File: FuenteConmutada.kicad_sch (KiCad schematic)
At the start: 9 parts, among them J2 Conn_01x02_Socket, P1 USB_C_Plug_USB2.0, U1 MT3608

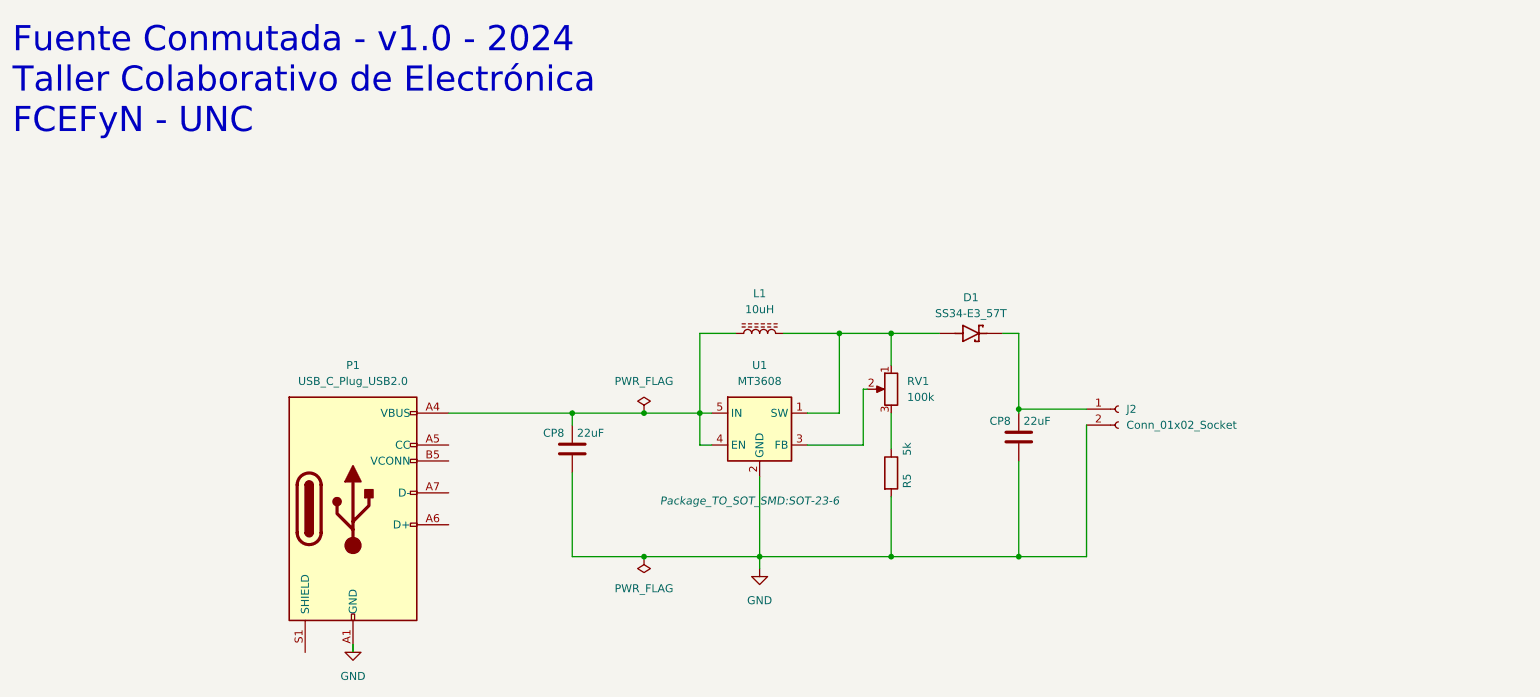
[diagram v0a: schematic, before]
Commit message: Esquematico 3in1 + Simbolo LMR64010 + Simu LT1930
Esquematico placa de prueba Boost-SEPIC-Fuente partida;
Simbolo para simulacion de LMR64010(xxx.asy debe estar en la misma carpeta);
Simulacion pasos del potenciometro, permite seleccionar el valor del pote(depende del valor de R2, L, RL)
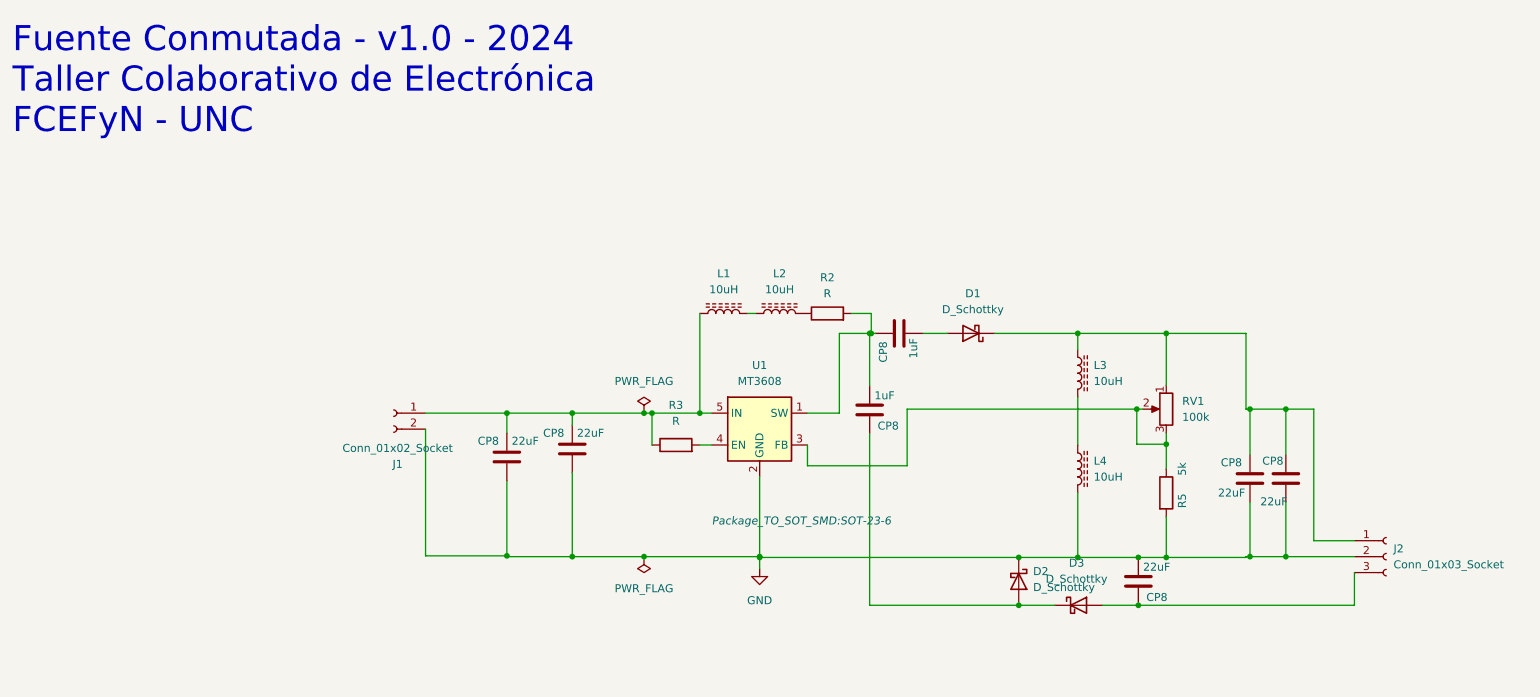
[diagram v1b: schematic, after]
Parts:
- removed D1: SS34-E3_57T, Diode_SMD:D_SMC_Handsoldering, symbol SS34-E3_57T:SS34-E3_57T
- removed J2: Conn_01x02_Socket, Connector_PinSocket_2.54mm:PinSocket_1x02_P2.54mm_Vertical, symbol Connector:Conn_01x02_Socket
- removed P1: USB_C_Plug_USB2.0, Connector_USB:USB_C_Receptacle_GCT_USB4105-xx-A_16P_TopMnt_Horizontal, symbol Connector:USB_C_Plug_USB2.0
- added CP8 (x2): 1uF, Capacitor_SMD:C_1206_3216Metric_Pad1.33x1.80mm_HandSolder, symbol Device:C
- added CP8 (x3): 22uF, Capacitor_SMD:C_1206_3216Metric_Pad1.33x1.80mm_HandSolder, symbol Device:C
- added D1, D2, D3: D_Schottky, Diode_SMD:D_SMA_Handsoldering, symbol Device:D_Schottky
- added J1: Conn_01x02_Socket, Connector_PinSocket_2.54mm:PinSocket_1x02_P2.54mm_Vertical, symbol Connector:Conn_01x02_Socket
- added J2: Conn_01x03_Socket, Connector_PinSocket_2.54mm:PinSocket_1x03_P2.54mm_Vertical, symbol Connector:Conn_01x03_Socket
- added L2, L3, L4: 10uH, Inductor_SMD:L_Taiyo-Yuden_NR-80xx_HandSoldering, symbol Device:L_Ferrite
- added R2, R3: R, Resistor_SMD:R_1206_3216Metric_Pad1.30x1.75mm_HandSolder, symbol Device:R
- RV1: footprint Potentiometer_THT:Potentiometer_Bourns_3299W_Vertical -> Potentiometer_THT:Potentiometer_Bourns_3299Y_Vertical
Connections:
- net GND: now also CP8.1, CP8.1, CP8.1, D2.1 (K), J1.2 (Pin_2), J2.2 (Pin_2), L4.2
- net at CP8.2: now also RV1.1, CP8.2, D1.1 (K), J2.1 (Pin_1), L3.1
- net at RV1.2, U1.3 (FB): now also R5.1, RV1.3
- net at CP8.2, L1.1, U1.5 (IN): now also CP8.2, J1.1 (Pin_1), R3.1; no longer U1.4 (EN)
- new net: L3.2, L4.1
- new net: CP8.1, CP8.2, R2.2, U1.1 (SW)
- new net: R3.2, U1.4 (EN)
- new net: CP8.2, D2.2 (A), D3.1 (K)
- new net: CP8.2, D3.2 (A), J2.3 (Pin_3)
- new net: CP8.1, D1.2 (A)
- new net: L1.2, L2.1
- new net: L2.2, R2.1
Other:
- moved on the sheet: CP8, L1, R5, RV1

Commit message: PCB
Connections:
- net Vo+: now reaches CP8.2, CP8.2, D1.1 (K), J2.1 (Pin_1), L3.1, RV1.1
- net Vin: now reaches CP8.2, CP8.2, J1.1 (Pin_1), L1.1, R3.1, U1.5 (IN)
- net Vo-: now reaches CP8.2, D3.2 (A), J2.3 (Pin_3)
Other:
- note added: "Inductor o Diodo (sepic o fuente partida)"
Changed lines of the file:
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@@
   (junction (at 200.025 63.5) (diameter 0) (color 0 0 0 0)
   )
+  (junction (at 219.075 99.06) (diameter 0) (color 0 0 0 0)
+  )
   (junction (at 105.41 76.2) (diameter 0) (color 0 0 0 0)
   )
@@
   (junction (at 176.53 99.187) (diameter 0) (color 0 0 0 0)
   )
-  (junction (at 219.075 99.06) (diameter 0) (color 0 0 0 0)
-  )
   (junction (at 125.73 76.2) (diameter 0) (color 0 0 0 0)
   )
@@
     (stroke (width 0) (type default))
   )
+  (wire (pts (xy 224.917 106.807) (xy 224.917 101.6))
+    (stroke (width 0) (type default))
+  )
   (wire (pts (xy 152.781 106.807) (xy 176.53 106.807))
     (stroke (width 0) (type default))
@@
     (stroke (width 0) (type default))
   )
+  (wire (pts (xy 125.73 60.325) (xy 125.73 76.2))
+    (stroke (width 0) (type default))
+  )
   (wire (pts (xy 105.41 76.2) (xy 116.84 76.2))
     (stroke (width 0) (type default))
   )
+  (wire (pts (xy 195.326 81.153) (xy 200.025 81.153))
+    (stroke (width 0) (type default))
+  )
+  (wire (pts (xy 94.996 86.995) (xy 94.996 98.933))
+    (stroke (width 0) (type default))
+  )
+  (wire (pts (xy 147.955 76.2) (xy 142.875 76.2))
+    (stroke (width 0) (type default))
+  )
+  (wire (pts (xy 185.928 63.5) (xy 200.025 63.5))
+    (stroke (width 0) (type default))
+  )
   (wire (pts (xy 219.075 99.06) (xy 229.997 99.06))
     (stroke (width 0) (type default))
   )
-  (wire (pts (xy 195.326 81.153) (xy 200.025 81.153))
-    (stroke (width 0) (type default))
-  )
-  (wire (pts (xy 94.996 86.995) (xy 94.996 98.933))
-    (stroke (width 0) (type default))
-  )
-  (wire (pts (xy 147.955 76.2) (xy 142.875 76.2))
-    (stroke (width 0) (type default))
-  )
-  (wire (pts (xy 185.928 63.5) (xy 200.025 63.5))
-    (stroke (width 0) (type default))
-  )
   (wire (pts (xy 185.928 73.66) (xy 185.928 81.28))
     (stroke (width 0) (type default))
@@
     (stroke (width 0) (type default))
   )
-  (wire (pts (xy 229.997 101.6) (xy 229.997 106.807))
+  (wire (pts (xy 224.917 106.807) (xy 195.58 106.807))
     (stroke (width 0) (type default))
   )
@@
     (stroke (width 0) (type default))
   )
-  (wire (pts (xy 229.997 106.807) (xy 195.58 106.807))
-    (stroke (width 0) (type default))
-  )
   (wire (pts (xy 94.996 76.2) (xy 94.996 79.375))
     (stroke (width 0) (type default))
@@
     (stroke (width 0) (type default))
   )
-  (wire (pts (xy 125.73 76.2) (xy 125.73 60.325))
-    (stroke (width 0) (type default))
-  )
   (wire (pts (xy 135.255 99.187) (xy 135.255 100.965))
     (stroke (width 0) (type default))
@@
   )
   (wire (pts (xy 118.11 76.2) (xy 118.11 81.28))
+    (stroke (width 0) (type default))
+  )
+  (wire (pts (xy 224.917 101.6) (xy 229.997 101.6))
     (stroke (width 0) (type default))
   )
@@
     (effects (font (size 4 4)) (justify left bottom))
   )
+  (text "Inductor o Diodo\n(sepic o fuente partida)" (at 168.656 90.932 0)
+    (effects (font (size 1.27 1.27)) (justify left bottom))
+  )
+  (label "Vo+" (at 227.203 96.52 0) (fields_autoplaced)
+    (effects (font (size 1.27 1.27)) (justify left bottom))
+  )
+  (label "Vin" (at 86.868 76.2 0) (fields_autoplaced)
+    (effects (font (size 1.27 1.27)) (justify left bottom))
+  )
+  (label "Vo-" (at 218.948 106.807 0) (fields_autoplaced)
+    (effects (font (size 1.27 1.27)) (justify left bottom))
+  )
   (symbol (lib_id "Device:L_Ferrite") (at 185.928 69.85 0) (unit 1)

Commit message: Cambios PCB+Esquematico
Huellas nuevas para inductores, diodos.
Correccion de diodo mal ubicado.
Se añadio R en serie con inductores 3 y 4, capacitor para compensacion, un segundo capacitor para salida Vo-.
Planos de GND, Vin, Vo+ y Vo-. Y tambien se agrandaron algunas pistas.
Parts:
- added CP8 (x2): 22uF, Capacitor_SMD:C_1206_3216Metric_Pad1.33x1.80mm_HandSolder, symbol Device:C
- added R4: R, Resistor_SMD:R_1206_3216Metric_Pad1.30x1.75mm_HandSolder, symbol Device:R
- D1, D2, D3: footprint Diode_SMD:D_SMA_Handsoldering -> Diode_SMD:D_SOD-128
- L1, L2, L3, L4: footprint Inductor_SMD:L_Taiyo-Yuden_NR-80xx_HandSoldering -> Inductor_SMD:L_Taiyo-Yuden_NR-40xx_HandSoldering
- RV1: footprint Potentiometer_THT:Potentiometer_Bourns_3299Y_Vertical -> Potentiometer_THT:Potentiometer_Bourns_3299W_Vertical
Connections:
- net GND: now also CP8.1, R4.1; no longer L4.2
- net Vo+: now also CP8.2; no longer L3.1
- net Vo-: now also CP8.2
- net at R5.1, RV1.2, RV1.3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: now also CP8.1
- net at CP8.1, D1.2 (A): now also L3.1
- new net: L4.2, R4.2
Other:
- moved on the sheet: D1, L4

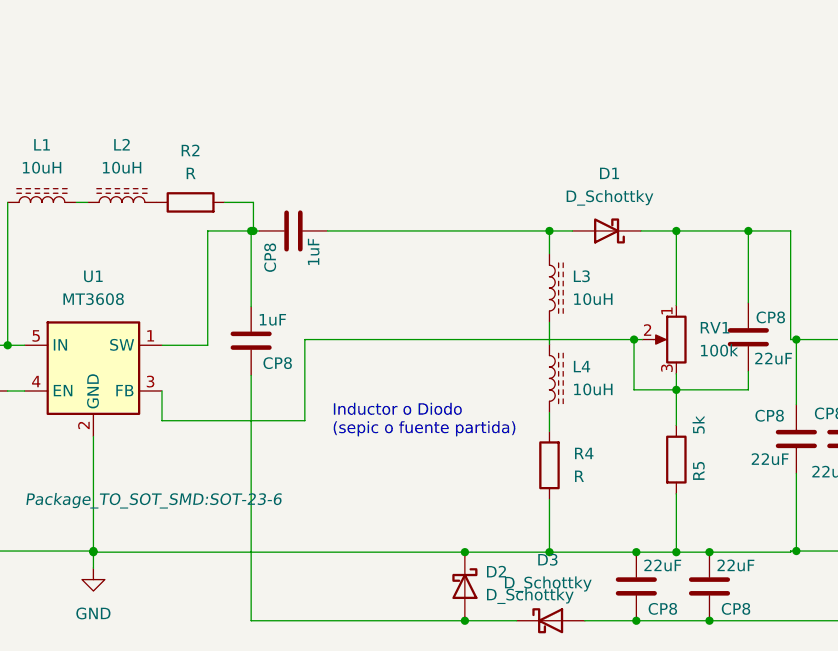
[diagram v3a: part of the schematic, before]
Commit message: PCB+Esquematico(actualizacion)
Se agrego R en serie con el diodo D1.
Y se habia agregado anteriormente una modificación sobre la huella del regulador.
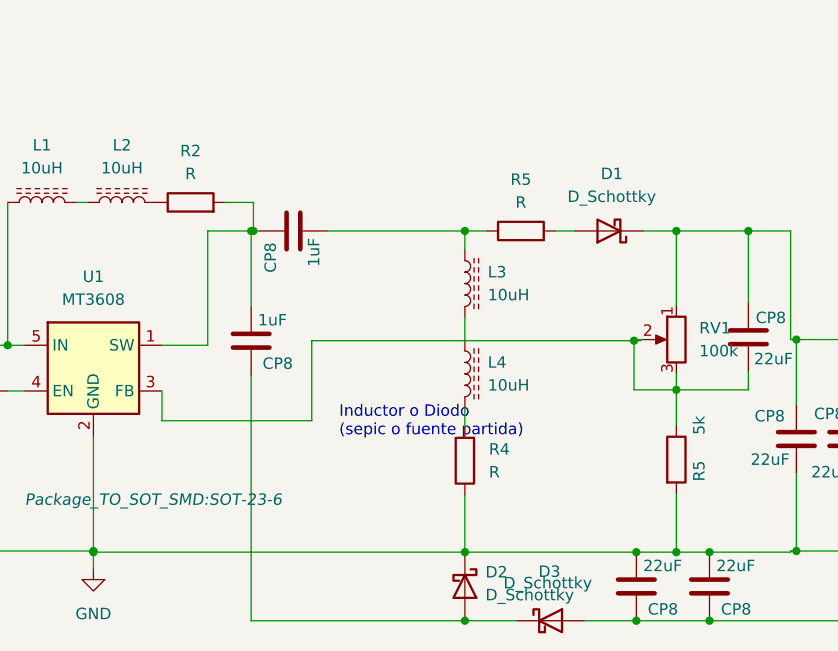
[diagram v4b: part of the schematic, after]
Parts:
- added R5: R, Resistor_SMD:R_1206_3216Metric_Pad1.30x1.75mm_HandSolder, symbol Device:R
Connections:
- net at CP8.1, L3.1: now also R5.1; no longer D1.2 (A)
- new net: D1.2 (A), R5.2
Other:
- moved on the sheet: L3, L4, R4
